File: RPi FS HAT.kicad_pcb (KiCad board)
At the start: 2 copper layers, 27.9 x 17.8 mm, 7 parts, among them J1 Raspberry_Pi_2_3, SW1 SW_DPST, U1 DHT22

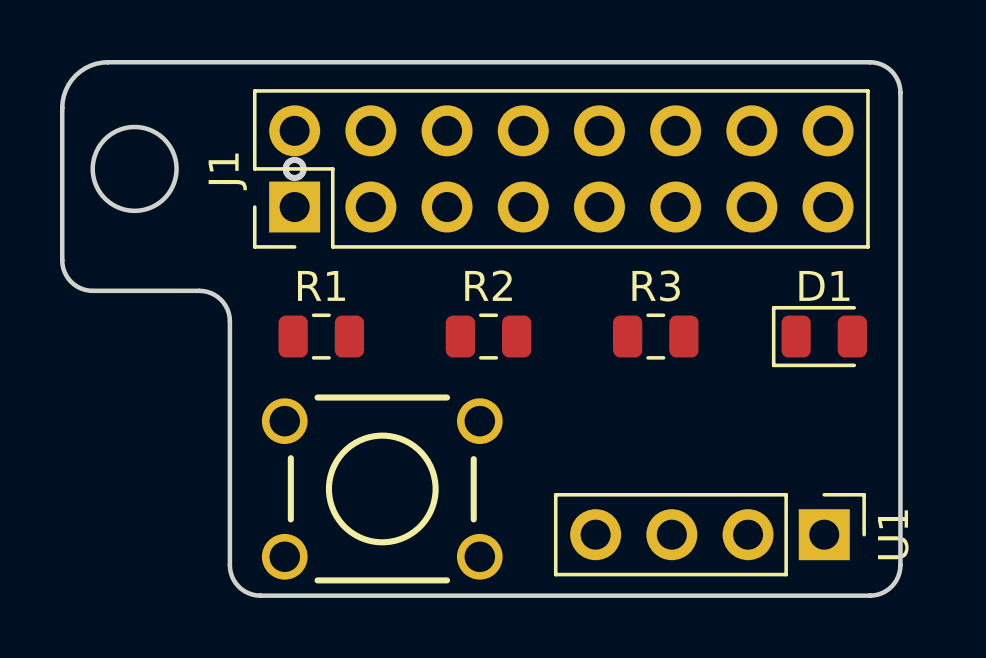
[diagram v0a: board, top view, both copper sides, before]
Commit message: Drawn tracks.
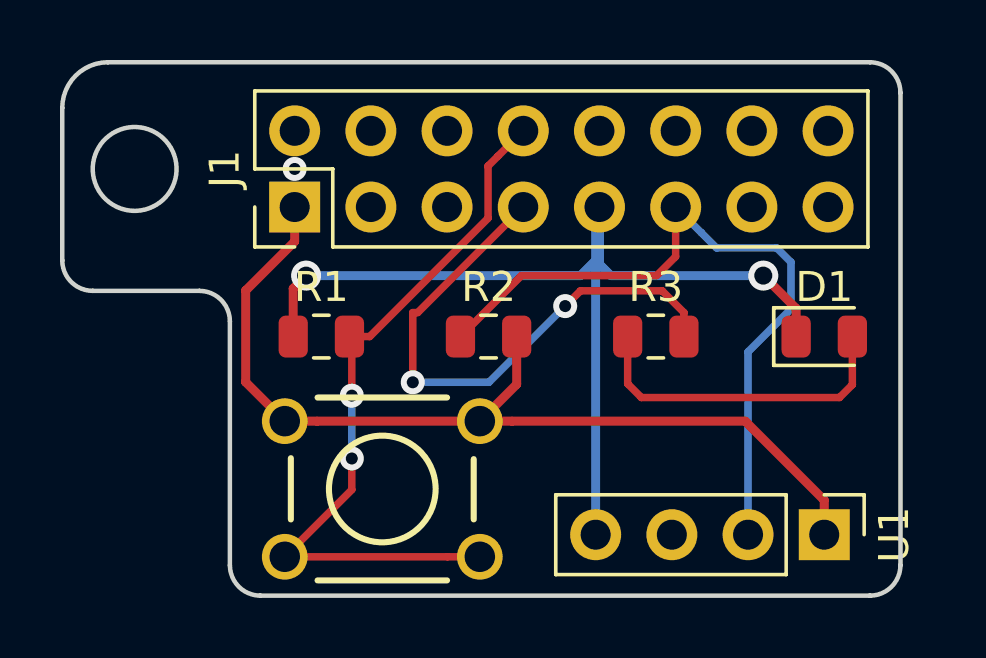
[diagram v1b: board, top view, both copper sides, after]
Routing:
- net GND: track 0.00 -> 34.9 mm, vias 0 -> 2
- net /3V3: track 0.00 -> 31.9 mm
- net /button_input: track 0.00 -> 24.5 mm, vias 0 -> 2
- net /sensor_data: track 0.00 -> 24.2 mm
- net /led: track 0.00 -> 18.9 mm, vias 0 -> 2
- net Net-(D1-Pad2): track 0.00 -> 11.0 mm
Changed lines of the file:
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@@
     (thickness 1.6)
     (drawings 13)
-    (tracks 1)
+    (tracks 69)
     (zones 0)
     (modules 7)
@@
   (gr_circle (center 142.621 116.84) (end 141.224 116.84) (layer Edge.Cuts) (width 0.15))
   (via (at 147.955 116.84) (size 0.8) (drill 0.4) (layers F.Cu B.Cu) (net 0))
+  (segment (start 157.988 118.237) (end 158.115 118.11) (width 0.3) (layer B.Cu) (net 1))
+  (segment (start 157.988 129.032) (end 157.988 118.237) (width 0.3) (layer B.Cu) (net 1))
+  (via (at 163.576 120.396) (size 1) (drill 0.6) (layers F.Cu B.Cu) (net 1))
+  (segment (start 164.6705 122.428) (end 164.6705 121.4905) (width 0.3) (layer F.Cu) (net 1))
+  (segment (start 164.6705 121.4905) (end 163.576 120.396) (width 0.3) (layer F.Cu) (net 1))
+  (segment (start 163.576 120.396) (end 158.496 120.396) (width 0.3) (layer B.Cu) (net 1))
+  (segment (start 158.115 120.015) (end 158.115 118.11) (width 0.3) (layer B.Cu) (net 1))
+  (segment (start 158.496 120.396) (end 158.115 120.015) (width 0.3) (layer B.Cu) (net 1))
+  (via (at 148.336 120.396) (size 1) (drill 0.6) (layers F.Cu B.Cu) (net 1))
+  (segment (start 147.9065 122.428) (end 147.9065 120.8255) (width 0.3) (layer F.Cu) (net 1))
+  (segment (start 147.9065 120.8255) (end 148.336 120.396) (width 0.3) (layer F.Cu) (net 1))
+  (segment (start 148.336 120.396) (end 157.48 120.396) (width 0.3) (layer B.Cu) (net 1))
+  (segment (start 158.115 119.761) (end 158.115 118.11) (width 0.3) (layer B.Cu) (net 1))
+  (segment (start 157.48 120.396) (end 158.115 119.761) (width 0.3) (layer B.Cu) (net 1))
+  (segment (start 166.5455 122.428) (end 166.5455 124.0305) (width 0.25) (layer F.Cu) (net 2))
+  (segment (start 166.5455 124.0305) (end 166.116 124.46) (width 0.25) (layer F.Cu) (net 2))
+  (segment (start 166.116 124.46) (end 159.512 124.46) (width 0.25) (layer F.Cu) (net 2))
+  (segment (start 159.055832 124.003832) (end 159.055832 122.428) (width 0.25) (layer F.Cu) (net 2))
+  (segment (start 159.512 124.46) (end 159.055832 124.003832) (width 0.25) (layer F.Cu) (net 2))
+  (segment (start 155.20483 125.2474) (end 154.1272 125.2474) (width 0.3) (layer F.Cu) (net 3))
+  (segment (start 162.9734 125.2474) (end 155.20483 125.2474) (width 0.3) (layer F.Cu) (net 3))
+  (segment (start 165.608 127.882) (end 162.9734 125.2474) (width 0.3) (layer F.Cu) (net 3))
+  (segment (start 165.608 129.032) (end 165.608 127.882) (width 0.3) (layer F.Cu) (net 3))
+  (segment (start 147.955 119.26) (end 147.955 118.11) (width 0.3) (layer F.Cu) (net 3))
+  (segment (start 146.32101 120.89399) (end 147.955 119.26) (width 0.3) (layer F.Cu) (net 3))
+  (segment (start 146.32101 123.94361) (end 146.32101 120.89399) (width 0.3) (layer F.Cu) (net 3))
+  (segment (start 147.6248 125.2474) (end 146.32101 123.94361) (width 0.3) (layer F.Cu) (net 3))
+  (segment (start 148.70243 125.2474) (end 154.1272 125.2474) (width 0.3) (layer F.Cu) (net 3))
+  (segment (start 147.6248 125.2474) (end 148.70243 125.2474) (width 0.3) (layer F.Cu) (net 3))
+  (segment (start 155.356166 124.018434) (end 154.1272 125.2474) (width 0.3) (layer F.Cu) (net 3))
+  (segment (start 155.356166 122.428) (end 155.356166 124.018434) (width 0.3) (layer F.Cu) (net 3))
+  (segment (start 160.930832 121.628) (end 160.206832 120.904) (width 0.25) (layer F.Cu) (net 8))
+  (segment (start 160.930832 122.428) (end 160.930832 121.628) (width 0.25) (layer F.Cu) (net 8))
+  (via (at 156.972 121.412) (size 0.8) (drill 0.4) (layers F.Cu B.Cu) (net 8))
+  (segment (start 160.206832 120.904) (end 157.48 120.904) (width 0.25) (layer F.Cu) (net 8))
+  (segment (start 157.48 120.904) (end 156.972 121.412) (width 0.25) (layer F.Cu) (net 8))
+  (via (at 151.892 123.952) (size 0.8) (drill 0.4) (layers F.Cu B.Cu) (net 8))
+  (segment (start 156.972 121.412) (end 154.432 123.952) (width 0.25) (layer B.Cu) (net 8))
+  (segment (start 154.432 123.952) (end 151.892 123.952) (width 0.25) (layer B.Cu) (net 8))
+  (segment (start 152.056588 121.628412) (end 155.575 118.11) (width 0.25) (layer F.Cu) (net 8))
+  (segment (start 151.892 123.952) (end 151.892 121.628412) (width 0.25) (layer F.Cu) (net 8))
+  (segment (start 151.892 121.628412) (end 152.056588 121.628412) (width 0.25) (layer F.Cu) (net 8))
+  (via (at 149.86 126.492) (size 0.8) (drill 0.4) (layers F.Cu B.Cu) (net 9))
+  (segment (start 147.6248 129.7686) (end 149.86 127.5334) (width 0.25) (layer F.Cu) (net 9))
+  (segment (start 149.86 127.5334) (end 149.86 126.492) (width 0.25) (layer F.Cu) (net 9))
+  (segment (start 149.86 126.492) (end 149.86 124.46) (width 0.25) (layer B.Cu) (net 9))
+  (via (at 149.86 124.3974) (size 0.8) (drill 0.4) (layers F.Cu B.Cu) (net 9))
+  (segment (start 149.86 124.46) (end 149.86 124.3974) (width 0.25) (layer B.Cu) (net 9))
+  (segment (start 149.86 122.5065) (end 149.7815 122.428) (width 0.25) (layer F.Cu) (net 9))
+  (segment (start 149.86 124.3974) (end 149.86 122.5065) (width 0.25) (layer F.Cu) (net 9))
+  (segment (start 154.725001 116.419999) (end 155.575 115.57) (width 0.25) (layer F.Cu) (net 9))
+  (segment (start 154.399999 116.745001) (end 154.725001 116.419999) (width 0.25) (layer F.Cu) (net 9))
+  (segment (start 154.399999 118.484003) (end 154.399999 116.745001) (width 0.25) (layer F.Cu) (net 9))
+  (segment (start 150.456002 122.428) (end 154.399999 118.484003) (width 0.25) (layer F.Cu) (net 9))
+  (segment (start 149.7815 122.428) (end 150.456002 122.428) (width 0.25) (layer F.Cu) (net 9))
+  (segment (start 153.04957 129.7686) (end 147.6248 129.7686) (width 0.25) (layer F.Cu) (net 9))
+  (segment (start 154.1272 129.7686) (end 153.04957 129.7686) (width 0.25) (layer F.Cu) (net 9))
+  (segment (start 160.655 119.761) (end 160.655 118.11) (width 0.25) (layer F.Cu) (net 11))
+  (segment (start 160.02 120.396) (end 160.655 119.761) (width 0.25) (layer F.Cu) (net 11))
+  (segment (start 153.481166 122.428) (end 155.513166 120.396) (width 0.25) (layer F.Cu) (net 11))
+  (segment (start 155.513166 120.396) (end 160.02 120.396) (width 0.25) (layer F.Cu) (net 11))
+  (segment (start 163.068 129.032) (end 163.068 122.936) (width 0.25) (layer B.Cu) (net 11))
+  (segment (start 164.501001 121.502999) (end 164.501001 119.951999) (width 0.25) (layer B.Cu) (net 11))
+  (segment (start 163.068 122.936) (end 164.501001 121.502999) (width 0.25) (layer B.Cu) (net 11))
+  (segment (start 161.504999 118.959999) (end 160.655 118.11) (width 0.25) (layer B.Cu) (net 11))
+  (segment (start 164.020001 119.470999) (end 162.015999 119.470999) (width 0.25) (layer B.Cu) (net 11))
+  (segment (start 162.015999 119.470999) (end 161.504999 118.959999) (width 0.25) (layer B.Cu) (net 11))
+  (segment (start 164.501001 119.951999) (end 164.020001 119.470999) (width 0.25) (layer B.Cu) (net 11))
 )

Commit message: Added back copper fill.
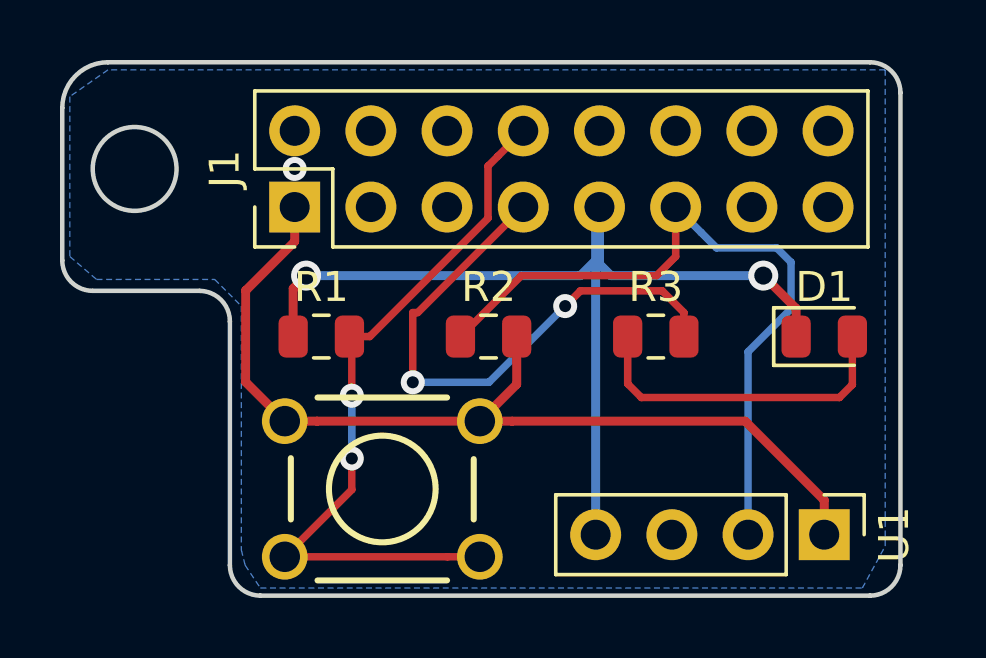
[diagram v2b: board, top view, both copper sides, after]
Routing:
- added copper zone on B.Cu, net GND
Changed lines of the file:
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@@
   (segment (start 162.015999 119.470999) (end 161.504999 118.959999) (width 0.25) (layer B.Cu) (net 11))
   (segment (start 164.501001 119.951999) (end 164.020001 119.470999) (width 0.25) (layer B.Cu) (net 11))
+  (zone (net 1) (net_name GND) (layer B.Cu) (hatch edge 0.508)
+    (connect_pads (clearance 0.508))
+    (min_thickness 0.254)
+    (fill yes (arc_segments 16) (thermal_gap 0.508) (thermal_bridge_width 0.508))
+    (polygon
+      (pts
+        (xy 167.64 113.538) (xy 141.732 113.538) (xy 140.462 114.427) (xy 140.462 119.761) (xy 141.351 120.523)
+        (xy 145.288 120.523) (xy 146.177 121.412) (xy 146.177 129.54) (xy 146.304 130.048) (xy 146.812 130.81)
+        (xy 166.878 130.81) (xy 167.64 129.413)
+      )
+    )
+  )
 )

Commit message: Added text silkscreen pabels to the front.
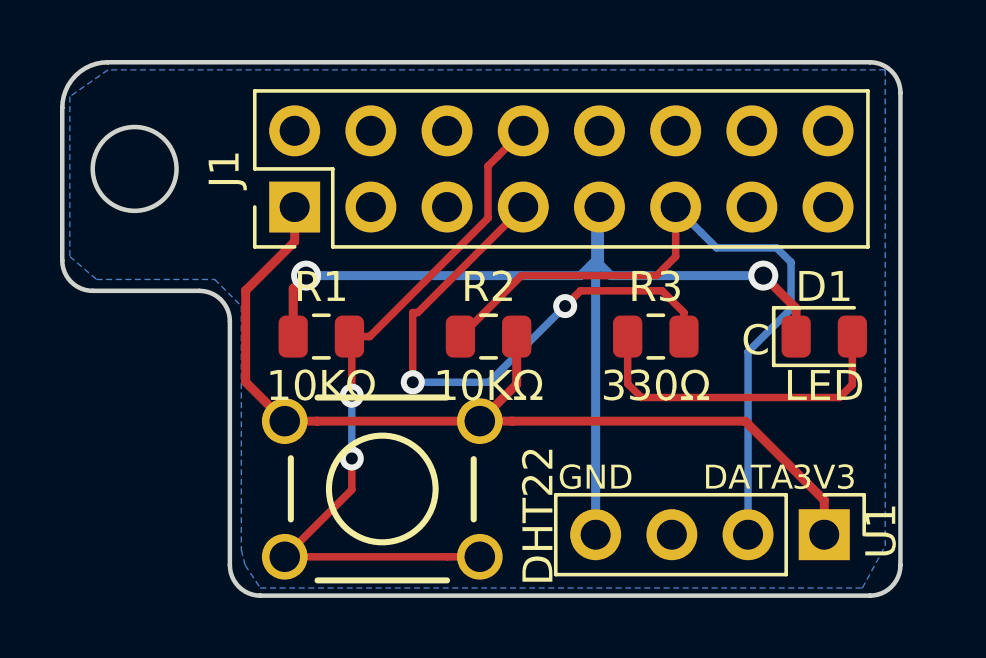
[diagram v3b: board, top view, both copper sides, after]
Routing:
- net (no net): vias 1 -> 0
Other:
- board text added: "3V3"
- board text added: "C"
- board text added: "DATA"
- board text added: "GND"
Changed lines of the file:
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@@
   (general
     (thickness 1.6)
-    (drawings 13)
-    (tracks 69)
+    (drawings 17)
+    (tracks 68)
     (zones 0)
     (modules 7)
@@
     (user_trace_width 0.3)
     (trace_clearance 0.2)
-    (zone_clearance 0.508)
+    (zone_clearance 0.54)
     (zone_45_only no)
     (trace_min 0.2)
@@
       (effects (font (size 1 1) (thickness 0.15)))
     )
-    (fp_text value LED (at 0 1.65) (layer F.Fab)
+    (fp_text value LED (at 0 1.65) (layer F.SilkS)
       (effects (font (size 1 1) (thickness 0.15)))
     )
@@
       (effects (font (size 1 1) (thickness 0.15)))
     )
-    (fp_text value 10KΩ (at 0 1.65) (layer F.Fab)
+    (fp_text value 10KΩ (at 0 1.65) (layer F.SilkS)
       (effects (font (size 1 1) (thickness 0.15)))
     )
@@
       (effects (font (size 1 1) (thickness 0.15)))
     )
-    (fp_text value 10KΩ (at 0 1.65) (layer F.Fab)
+    (fp_text value 10KΩ (at 0 1.65) (layer F.SilkS)
       (effects (font (size 1 1) (thickness 0.15)))
     )
@@
       (effects (font (size 1 1) (thickness 0.15)))
     )
-    (fp_text value 330Ω (at 0 1.65) (layer F.Fab)
+    (fp_text value 330Ω (at 0 1.65) (layer F.SilkS)
       (effects (font (size 1 1) (thickness 0.15)))
     )
@@
     (descr "Through hole straight pin header, 1x04, 2.54mm pitch, single row")
     (tags "Through hole pin header THT 1x04 2.54mm single row")
-    (fp_text reference U1 (at 0 -2.33 270) (layer F.SilkS)
-      (effects (font (size 1 1) (thickness 0.15)))
-    )
-    (fp_text value DHT22 (at 0 9.95 270) (layer F.Fab)
+    (fp_text reference U1 (at -0.127 -1.905 270) (layer F.SilkS)
+      (effects (font (size 1 1) (thickness 0.15)))
+    )
+    (fp_text value DHT22 (at -0.635 9.525 270) (layer F.SilkS)
       (effects (font (size 1 1) (thickness 0.15)))
     )
@@
     )
   )
+  (gr_text GND (at 157.988 127.127) (layer F.SilkS)
+    (effects (font (size 0.8 0.8) (thickness 0.2)))
+  )
+  (gr_text DATA (at 163.068 127.127) (layer F.SilkS)
+    (effects (font (size 0.8 0.8) (thickness 0.2)))
+  )
+  (gr_text 3V3 (at 165.608 127.127) (layer F.SilkS)
+    (effects (font (size 0.8 0.8) (thickness 0.2)))
+  )
+  (gr_text C (at 163.322 122.555) (layer F.SilkS)
+    (effects (font (size 1 1) (thickness 0.25)))
+  )
   (gr_line (start 168.148 114.3) (end 168.148 130.048) (layer Edge.Cuts) (width 0.15))
   (gr_line (start 146.812 131.064) (end 167.132 131.064) (layer Edge.Cuts) (width 0.15))
@@
   (gr_arc (start 141.732 114.808) (end 141.732 113.284) (angle -90) (layer Edge.Cuts) (width 0.15))
   (gr_circle (center 142.621 116.84) (end 141.224 116.84) (layer Edge.Cuts) (width 0.15))
-  (via (at 147.955 116.84) (size 0.8) (drill 0.4) (layers F.Cu B.Cu) (net 0))
   (segment (start 157.988 118.237) (end 158.115 118.11) (width 0.3) (layer B.Cu) (net 1))
   (segment (start 157.988 129.032) (end 157.988 118.237) (width 0.3) (layer B.Cu) (net 1))
@@
   (segment (start 164.501001 119.951999) (end 164.020001 119.470999) (width 0.25) (layer B.Cu) (net 11))
   (zone (net 1) (net_name GND) (layer B.Cu) (hatch edge 0.508)
-    (connect_pads (clearance 0.508))
+    (connect_pads (clearance 0.54))
     (min_thickness 0.254)
     (fill yes (arc_segments 16) (thermal_gap 0.508) (thermal_bridge_width 0.508))

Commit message: Added Gerbers, completed project.
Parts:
- added G***: LOGO, Custom libraries:TE_Logo_12mm, B.Cu at (152.7, 121.7)
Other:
- board text added: "Button: GPIO14 LED: GPIO4"
- board text added: "Raspberry Pi Full Stack Version 2"
- board text added: "peter@txplore.com"
